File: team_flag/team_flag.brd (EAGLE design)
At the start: 40.6 x 40.6 mm, 11 parts, among them Q1 MOSFET-LOGIC-NCHANNELSMD, Q2 MOSFET-LOGIC-NCHANNELSMD

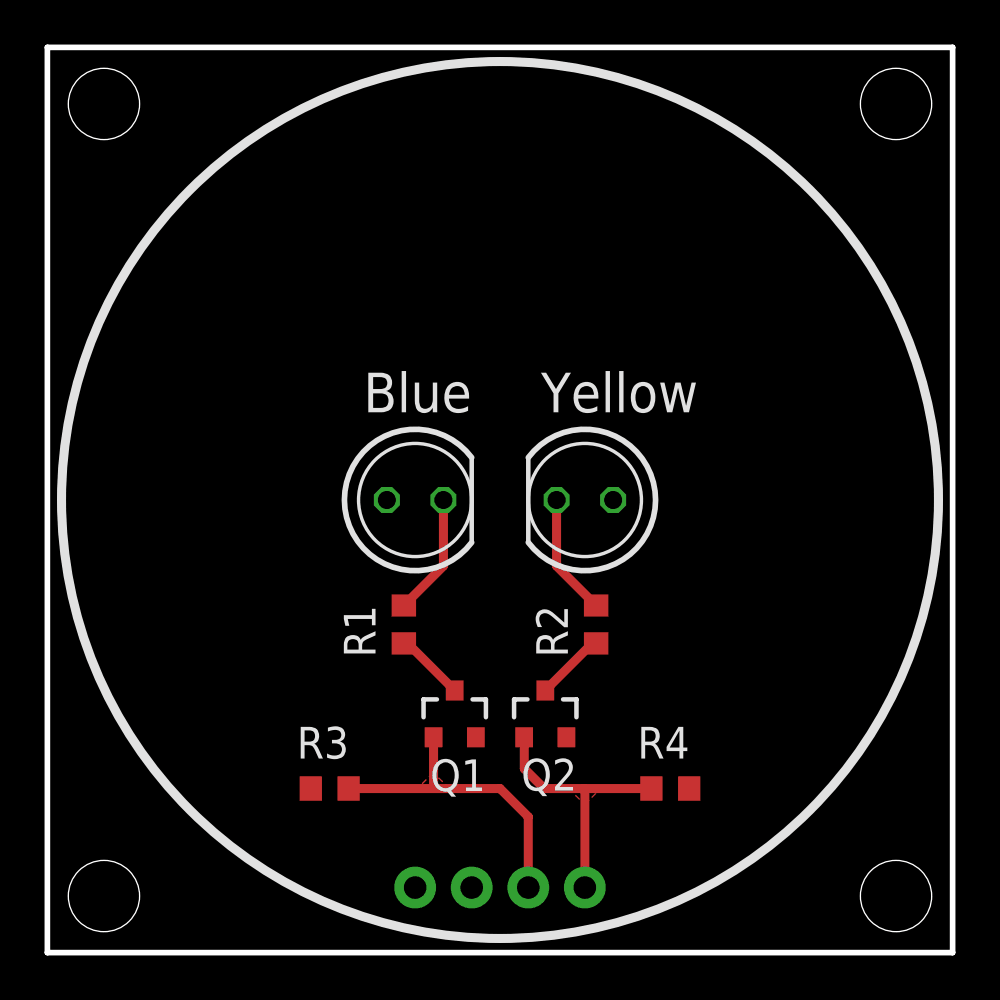
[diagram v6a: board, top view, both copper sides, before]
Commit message: Team flag silk changes as per Casey and Aravind's requests
changed resistor values to 200 ohm, new LED footprint to show which
side is anode/cathode, maybe other silkscreen changes?

Basically, this is Sumita's Team Flag, but with my new LED footprint
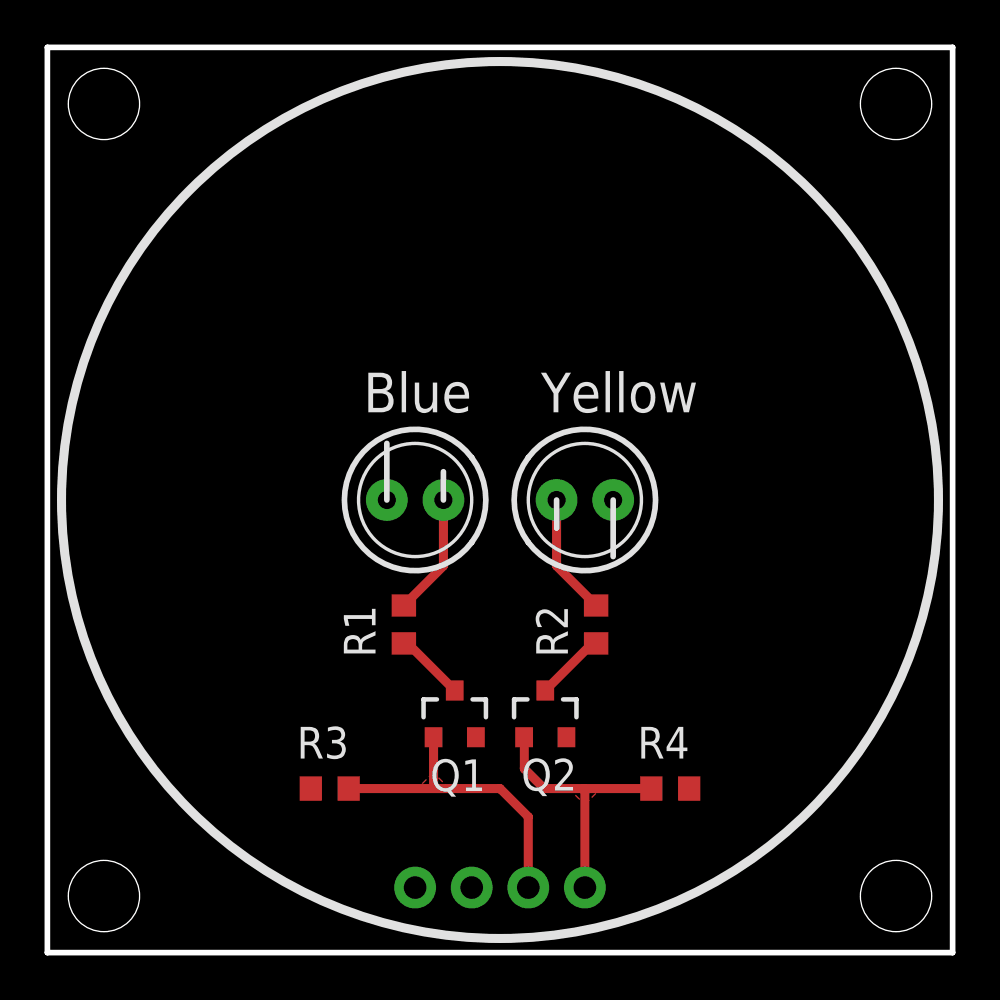
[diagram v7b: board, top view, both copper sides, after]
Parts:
- LED1, LED2: device led:LED5MM -> pie:LED5MM-NOFLAT
- turned JP1 to 180 degrees
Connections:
- net BLUE: now also JP1.3; no longer JP1.2
- net GND: now also JP1.1; no longer JP1.4
- net VCC: now also JP1.2; no longer JP1.3
- net YELLOW: now also JP1.4; no longer JP1.1
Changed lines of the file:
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@@
 <setting verticaltext="up"/>
 </settings>
-<grid distance="1" unitdist="mil" unit="inch" style="lines" multiple="1" display="yes" altdistance="0.025" altunitdist="inch" altunit="inch"/>
+<grid distance="0.001" unitdist="inch" unit="inch" style="lines" multiple="1" display="yes" altdistance="0.025" altunitdist="inch" altunit="inch"/>
 <layers>
 <layer number="1" name="Top" color="4" fill="1" visible="yes" active="yes"/>
@@
 <layer number="24" name="bOrigins" color="15" fill="1" visible="yes" active="yes"/>
 <layer number="25" name="tNames" color="7" fill="1" visible="yes" active="yes"/>
-<layer number="26" name="bNames" color="7" fill="1" visible="yes" active="yes"/>
+<layer number="26" name="bNames" color="14" fill="1" visible="yes" active="yes"/>
 <layer number="27" name="tValues" color="7" fill="1" visible="yes" active="yes"/>
-<layer number="28" name="bValues" color="7" fill="1" visible="yes" active="yes"/>
+<layer number="28" name="bValues" color="14" fill="1" visible="yes" active="yes"/>
 <layer number="29" name="tStop" color="7" fill="3" visible="yes" active="yes"/>
 <layer number="30" name="bStop" color="7" fill="6" visible="yes" active="yes"/>
@@
 <layer number="97" name="Info" color="7" fill="1" visible="no" active="no"/>
 <layer number="98" name="Guide" color="6" fill="1" visible="no" active="no"/>
+<layer number="99" name="SpiceOrder" color="5" fill="1" visible="no" active="no"/>
 <layer number="100" name="Muster" color="7" fill="1" visible="no" active="no"/>
 <layer number="101" name="Patch_Top" color="12" fill="4" visible="yes" active="yes"/>
@@
 </autorouter>
 <elements>
-<element name="LED1" library="led" package="LED5MM" value="" x="16.51" y="20.32" smashed="yes">
+<element name="LED1" library="pie" package="LED5MM-NOFLAT" value="" x="16.51" y="20.32" smashed="yes">
 <attribute name="VALUE" x="19.7104" y="18.5166" size="1.27" layer="27" ratio="10"/>
 </element>
-<element name="LED2" library="led" package="LED5MM" value="" x="24.13" y="20.32" smashed="yes" rot="R180">
+<element name="LED2" library="pie" package="LED5MM-NOFLAT" value="" x="24.13" y="20.32" smashed="yes" rot="R180">
 <attribute name="VALUE" x="20.9296" y="22.1234" size="1.27" layer="27" ratio="10" rot="R180"/>
 </element>
@@
 <attribute name="VALUE" x="26.4922" y="4.6228" size="1.4224" layer="27" font="vector" rot="R180" align="top-right"/>
 </element>
-<element name="JP1" library="pie" package="1X04-MTA" value="" x="20.32" y="2.921" smashed="yes" rot="MR0">
-<attribute name="PARTNUMBER" value="A1922-ND" x="20.32" y="2.921" size="1.778" layer="28" rot="MR0" display="off"/>
-<attribute name="VALUE" x="24.765" y="-1.524" size="1.27" layer="28" font="vector" rot="MR0"/>
+<element name="JP1" library="pie" package="1X04-MTA" value="" x="20.32" y="2.921" smashed="yes" rot="MR180">
+<attribute name="PARTNUMBER" value="A1922-ND" x="20.32" y="2.921" size="1.778" layer="28" rot="MR180" display="off"/>
+<attribute name="VALUE" x="15.875" y="7.366" size="1.27" layer="28" font="vector" rot="MR180"/>
 </element>
 </elements>
@@
 </polygon>
 <wire x1="24.13" y1="7.3406" x2="24.1046" y2="7.366" width="0.4064" layer="1"/>
-<contactref element="JP1" pad="1"/>
-<wire x1="24.13" y1="2.921" x2="24.13" y2="7.3406" width="0.4064" layer="1"/>
+<contactref element="JP1" pad="4"/>
+<wire x1="24.13" y1="7.3406" x2="24.13" y2="2.921" width="0.4064" layer="1"/>
 </signal>
 <signal name="VCC">
@@
 <contactref element="LED1" pad="A"/>
 <contactref element="LED2" pad="A"/>
-<contactref element="JP1" pad="3"/>
+<contactref element="JP1" pad="2"/>
 </signal>
 <signal name="GND">
@@
 <contactref element="Q1" pad="2"/>
 <contactref element="Q2" pad="2"/>
-<contactref element="JP1" pad="4"/>
+<contactref element="JP1" pad="1"/>
 </signal>
 <signal name="BLUE">
@@
 <vertex x="16.6116" y="7.366"/>
 </polygon>
-<contactref element="JP1" pad="2"/>
+<contactref element="JP1" pad="3"/>
 <wire x1="21.59" y1="6.096" x2="21.59" y2="2.921" width="0.4064" layer="1"/>
 </signal>

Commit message: set resistor values (on Team flag) to 200 ohms
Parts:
- R1, R2: value 330 -> 200
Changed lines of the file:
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@@
 <attribute name="VALUE" x="20.9296" y="22.1234" size="1.27" layer="27" ratio="10" rot="R180"/>
 </element>
-<element name="R1" library="rcl" package="R0603" value="330" x="16.002" y="14.732" smashed="yes" rot="R90">
+<element name="R1" library="rcl" package="R0603" value="200" x="16.002" y="14.732" smashed="yes" rot="R90">
 <attribute name="NAME" x="14.732" y="13.2588" size="1.4224" layer="25" font="vector" rot="R90"/>
 <attribute name="VALUE" x="17.272" y="13.2588" size="1.4224" layer="27" font="vector" rot="R270" align="bottom-right"/>
 </element>
-<element name="R2" library="rcl" package="R0603" value="330" x="24.638" y="14.732" smashed="yes" rot="R90">
+<element name="R2" library="rcl" package="R0603" value="200" x="24.638" y="14.732" smashed="yes" rot="R90">
 <attribute name="NAME" x="23.368" y="13.2588" size="1.4224" layer="25" font="vector" rot="R90"/>
 <attribute name="VALUE" x="25.8826" y="13.2588" size="1.4224" layer="27" font="vector" rot="R270" align="bottom-right"/>
